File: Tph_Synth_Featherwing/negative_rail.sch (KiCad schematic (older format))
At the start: 0 parts

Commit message: Add LM2663 Negative voltage generator
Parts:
- added U?: LM2663M, SOIC127P620X175-8N, symbol LM2663M:LM2663M
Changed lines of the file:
@@
 $Descr A4 11693 8268
 encoding utf-8
-Sheet 1 5
+Sheet 3 5
 Title ""
 Date ""
@@
 Comment4 ""
 $EndDescr
+$Comp
+L LM2663M:LM2663M U?
+U 1 1 5DCC03A8
+P 5515 3250
+F 0 "U?" H 5515 3915 50  0000 C CNN
+F 1 "LM2663M" H 5515 3824 50  0000 C CNN
+F 2 "SOIC127P620X175-8N" H 5515 3250 50  0001 L BNN
+F 3 "Unavailable" H 5515 3250 50  0001 L BNN
+F 4 "None" H 5515 3250 50  0001 L BNN "Field4"
+F 5 "Charge Pump INV/STPUP/STPDN -1.5V to -5.5V 200mA 8-Pin SOIC N Rail" H 5515 3250 50  0001 L BNN "Field5"
+F 6 "SOIC-8 Texas Instruments" H 5515 3250 50  0001 L BNN "Field6"
+F 7 "LM2663M" H 5515 3250 50  0001 L BNN "Field7"
+F 8 "Texas Instruments" H 5515 3250 50  0001 L BNN "Field8"
+	1    5515 3250
+	1    0    0    -1
+$EndComp
 $EndSCHEMATC

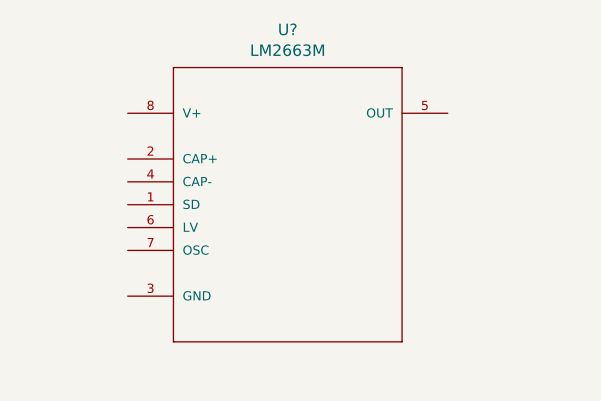
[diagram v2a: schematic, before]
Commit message: Add parts for voltage inverter
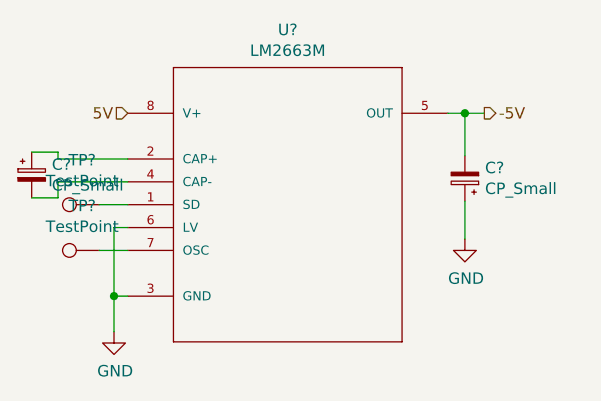
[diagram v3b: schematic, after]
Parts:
- added C? (x2): CP_Small, symbol Device:CP_Small
- added TP? (x2): TestPoint, symbol Connector:TestPoint
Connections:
- net at U?.1 (SD): now also TP?.1
- net at U?.2 (CAP+): now also C?.1
- net GND: now reaches U?.3 (GND)
- net GND: now also U?.6 (LV), C?.1
- net at U?.4 (CAP-): now also C?.2
- net -5V: now reaches U?.5 (OUT)
- net -5V: now also C?.2
- net at U?.7 (OSC): now also TP?.1
- net 5V: now reaches U?.8 (V+)

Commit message: Progress on sub-sheet labels and boost converter
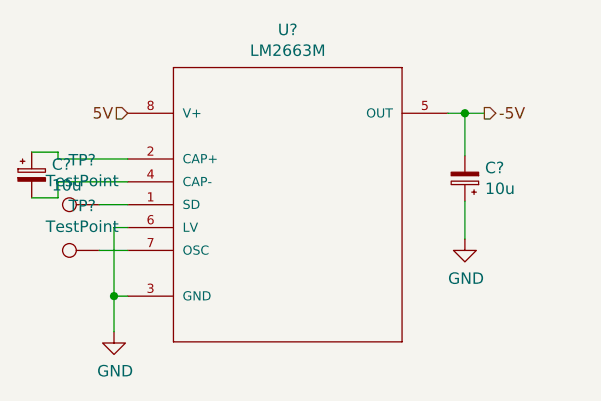
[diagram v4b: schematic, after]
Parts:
- C? (x2): value CP_Small -> 10u
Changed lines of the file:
@@
 Data
 89 50 4E 47 0D 0A 1A 0A 00 00 00 0D 49 48 44 52 00 00 03 E3 00 00 02 79 08 02 00 00 00 4A 6C 76
-16 00 00 00 03 73 42 49 54 08 08 08 DB E1 4F E0 00 00 00 09 70 48 59 73 00 00 12 74 00 00 12 74
-01 DE 66 1F 78 00 00 20 00 49 44 41 54 78 9C EC DD 79 B4 1C E5 79 2E FA E7 1B AA AA 87 3D 6B 9E
+16 00 00 00 03 73 42 49 54 08 08 08 DB E1 4F E0 00 00 00 09 70 48 59 73 00 00 12 5C 00 00 12 5C
+01 68 C4 36 89 00 00 20 00 49 44 41 54 78 9C EC DD 79 B4 1C E5 79 2E FA E7 1B AA AA 87 3D 6B 9E
 25 10 12 12 48 42 60 E6 19 1B 63 B0 8D 0D D8 D8 D8 B1 93 9C 0C C4 37 5E CE 75 A6 9B EB AC EB B3
 CE 90 C4 E7 9C 9B DC 75 1C E7 D8 CE B2 4D 3C 0F 80 C1 C6 18 9B 51 08 10 42 62 90 04 92 40 12 9A
@@
 P 4395 3220
 F 0 "C?" H 4483 3266 50  0000 L CNN
-F 1 "CP_Small" H 4483 3175 50  0000 L CNN
+F 1 "10u" H 4483 3175 50  0000 L CNN
 F 2 "" H 4395 3220 50  0001 C CNN
 F 3 "~" H 4395 3220 50  0001 C CNN
@@
 P 6290 3235
 F 0 "C?" H 6202 3189 50  0000 R CNN
-F 1 "CP_Small" H 6202 3280 50  0000 R CNN
+F 1 "10u" H 6202 3280 50  0000 R CNN
 F 2 "" H 6290 3235 50  0001 C CNN
 F 3 "~" H 6290 3235 50  0001 C CNN
@@
 $EndComp
 $Comp
-L power:GND #PWR?
+L power:GND #PWR01
 U 1 1 5DED0485
 P 4755 3905
-F 0 "#PWR?" H 4755 3655 50  0001 C CNN
+F 0 "#PWR01" H 4755 3655 50  0001 C CNN
 F 1 "GND" H 4760 3732 50  0000 C CNN
 F 2 "" H 4755 3905 50  0001 C CNN
@@
 $EndComp
 $Comp
-L power:GND #PWR?
+L power:GND #PWR02
 U 1 1 5DED04A1
 P 6290 3500
-F 0 "#PWR?" H 6290 3250 50  0001 C CNN
+F 0 "#PWR02" H 6290 3250 50  0001 C CNN
 F 1 "GND" H 6295 3327 50  0000 C CNN
 F 2 "" H 6290 3500 50  0001 C CNN

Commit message: Added first-cut of schematic
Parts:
- gave numbers to parts that had none: 5
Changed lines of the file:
@@
 $EndDescr
 $Comp
-L LM2663M:LM2663M U?
+L LM2663M:LM2663M U2
 U 1 1 5DCC03A8
 P 5515 3250
-F 0 "U?" H 5515 3915 50  0000 C CNN
+F 0 "U2" H 5515 3915 50  0000 C CNN
 F 1 "LM2663M" H 5515 3824 50  0000 C CNN
 F 2 "SOIC127P620X175-8N" H 5515 3250 50  0001 L BNN
@@
 $EndBitmap
 $Comp
-L Device:CP_Small C?
+L Device:CP_Small C4
 U 1 1 5DECFC94
 P 4395 3220
-F 0 "C?" H 4483 3266 50  0000 L CNN
+F 0 "C4" H 4483 3266 50  0000 L CNN
 F 1 "10u" H 4483 3175 50  0000 L CNN
 F 2 "" H 4395 3220 50  0001 C CNN
@@
 $EndComp
 $Comp
-L Device:CP_Small C?
+L Device:CP_Small C5
 U 1 1 5DECFDD1
 P 6290 3235
-F 0 "C?" H 6202 3189 50  0000 R CNN
+F 0 "C5" H 6202 3189 50  0000 R CNN
 F 1 "10u" H 6202 3280 50  0000 R CNN
 F 2 "" H 6290 3235 50  0001 C CNN
@@
 $EndComp
 $Comp
-L Connector:TestPoint TP?
+L Connector:TestPoint TP2
 U 1 1 5DED0082
 P 4690 3550
-F 0 "TP?" V 4885 3624 50  0000 C CNN
+F 0 "TP2" V 4885 3624 50  0000 C CNN
 F 1 "TestPoint" V 4794 3624 50  0000 C CNN
 F 2 "" H 4890 3550 50  0001 C CNN
@@
 $EndComp
 $Comp
-L Connector:TestPoint TP?
+L Connector:TestPoint TP1
 U 1 1 5DED027A
 P 4690 3350
-F 0 "TP?" V 4885 3424 50  0000 C CNN
+F 0 "TP1" V 4885 3424 50  0000 C CNN
 F 1 "TestPoint" V 4794 3424 50  0000 C CNN
 F 2 "" H 4890 3350 50  0001 C CNN

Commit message: Initial attempt at PCB
Signed-off-by: Tisham Dhar <whatnickd@gmail.com>
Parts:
- C4, C5: footprint (none) -> Capacitor_SMD:C_0805_2012Metric
- TP1, TP2: footprint (none) -> TestPoint:TestPoint_Pad_D1.0mm
- U2: footprint SOIC127P620X175-8N -> Package_SO:SOIC-8_3.9x4.9mm_P1.27mm
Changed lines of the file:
@@
 F 0 "U2" H 5515 3915 50  0000 C CNN
 F 1 "LM2663M" H 5515 3824 50  0000 C CNN
-F 2 "SOIC127P620X175-8N" H 5515 3250 50  0001 L BNN
+F 2 "Package_SO:SOIC-8_3.9x4.9mm_P1.27mm" H 5515 3250 50  0001 L BNN
 F 3 "Unavailable" H 5515 3250 50  0001 L BNN
 F 4 "None" H 5515 3250 50  0001 L BNN "Field4"
@@
 F 0 "C4" H 4483 3266 50  0000 L CNN
 F 1 "10u" H 4483 3175 50  0000 L CNN
-F 2 "" H 4395 3220 50  0001 C CNN
+F 2 "Capacitor_SMD:C_0805_2012Metric" H 4395 3220 50  0001 C CNN
 F 3 "~" H 4395 3220 50  0001 C CNN
 	1    4395 3220
@@
 F 0 "C5" H 6202 3189 50  0000 R CNN
 F 1 "10u" H 6202 3280 50  0000 R CNN
-F 2 "" H 6290 3235 50  0001 C CNN
+F 2 "Capacitor_SMD:C_0805_2012Metric" H 6290 3235 50  0001 C CNN
 F 3 "~" H 6290 3235 50  0001 C CNN
 	1    6290 3235
@@
 F 0 "TP2" V 4885 3624 50  0000 C CNN
 F 1 "TestPoint" V 4794 3624 50  0000 C CNN
-F 2 "" H 4890 3550 50  0001 C CNN
+F 2 "TestPoint:TestPoint_Pad_D1.0mm" H 4890 3550 50  0001 C CNN
 F 3 "~" H 4890 3550 50  0001 C CNN
 	1    4690 3550
@@
 F 0 "TP1" V 4885 3424 50  0000 C CNN
 F 1 "TestPoint" V 4794 3424 50  0000 C CNN
-F 2 "" H 4890 3350 50  0001 C CNN
+F 2 "TestPoint:TestPoint_Pad_D1.0mm" H 4890 3350 50  0001 C CNN
 F 3 "~" H 4890 3350 50  0001 C CNN
 	1    4690 3350

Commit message: Added BOM and upgraded to kicad 5.0
Signed-off-by: Tisham Dhar <whatnickd@gmail.com>
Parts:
- C4, C5: manf# (none) -> GMK212BBJ106MG-T
- TP1, TP2: DNP (none) -> (none)
- U2: manf# (none) -> LM2663MX/NOPB
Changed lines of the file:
@@
 EESchema Schematic File Version 4
-LIBS:Tph_Synth_Featherwing-cache
-EELAYER 26 0
+EELAYER 30 0
 EELAYER END
 $Descr A4 11693 8268
@@
 F 7 "LM2663M" H 5515 3250 50  0001 L BNN "Field7"
 F 8 "Texas Instruments" H 5515 3250 50  0001 L BNN "Field8"
+F 9 "LM2663MX/NOPB" H 5515 3250 50  0001 C CNN "manf#"
 	1    5515 3250
 	1    0    0    -1
@@
 F 2 "Capacitor_SMD:C_0805_2012Metric" H 4395 3220 50  0001 C CNN
 F 3 "~" H 4395 3220 50  0001 C CNN
+F 4 "GMK212BBJ106MG-T" H 4395 3220 50  0001 C CNN "manf#"
 	1    4395 3220
 	1    0    0    -1
@@
 F 2 "Capacitor_SMD:C_0805_2012Metric" H 6290 3235 50  0001 C CNN
 F 3 "~" H 6290 3235 50  0001 C CNN
+F 4 "GMK212BBJ106MG-T" H 6290 3235 50  0001 C CNN "manf#"
 	1    6290 3235
 	-1   0    0    1
@@
 F 2 "TestPoint:TestPoint_Pad_D1.0mm" H 4890 3550 50  0001 C CNN
 F 3 "~" H 4890 3550 50  0001 C CNN
+F 4 " " H 4690 3550 50  0001 C CNN "DNP"
 	1    4690 3550
 	0    -1   -1   0
@@
 F 2 "TestPoint:TestPoint_Pad_D1.0mm" H 4890 3350 50  0001 C CNN
 F 3 "~" H 4890 3350 50  0001 C CNN
+F 4 " " H 4690 3350 50  0001 C CNN "DNP"
 	1    4690 3350
 	0    -1   -1   0
